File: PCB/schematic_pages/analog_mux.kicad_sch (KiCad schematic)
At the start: 33 parts, among them U1 SS49E, U10 SS49E, U11 SS49E, U12 SS49E, U13 SS49E, U3 SS49E, U4 SS49E, U5 SS49E, U6 SS49E, U7 SS49E, U8 SS49E, U9 SS49E

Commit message: repo rearrange
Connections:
- net MUX_IN_0 renamed AMUX_S0
- net MUX_IN_1 renamed AMUX_S1
- net MUX_IN_2 renamed AMUX_S2
- net MUX_IN_3 renamed AMUX_S3
- net MUX_OUT renamed AMUX_OUT
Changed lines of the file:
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@@
 		)
 	)
-	(global_label "MUX_IN_1"
+	(hierarchical_label "AMUX_OUT"
 		(shape input)
-		(at 25.4 102.87 180)
-		(fields_autoplaced yes)
+		(at 25.4 90.17 180)
 		(effects
 			(font
@@
 			(justify right)
 		)
-		(property "Intersheetrefs" "${INTERSHEET_REFS}"
-			(at 13.3434 102.87 0)
-			(effects
-				(font
-					(size 1.27 1.27)
-				)
-				(justify right)
-				(hide yes)
-			)
-		)
 	)
-	(global_label "MUX_OUT"
+	(hierarchical_label "AMUX_S1"
 		(shape input)
-		(at 25.4 90.17 180)
-		(fields_autoplaced yes)
+		(at 25.4 102.87 180)
 		(effects
 			(font
@@
 			(justify right)
 		)
-		(property "Intersheetrefs" "${INTERSHEET_REFS}"
-			(at 13.8272 90.17 0)
-			(effects
-				(font
-					(size 1.27 1.27)
-				)
-				(justify right)
-				(hide yes)
-			)
-		)
 	)
-	(global_label "MUX_IN_0"
+	(hierarchical_label "AMUX_S0"
 		(shape input)
 		(at 25.4 100.33 180)
-		(fields_autoplaced yes)
 		(effects
 			(font
@@
 			(justify right)
 		)
-		(property "Intersheetrefs" "${INTERSHEET_REFS}"
-			(at 13.3434 100.33 0)
-			(effects
-				(font
-					(size 1.27 1.27)
-				)
-				(justify right)
-				(hide yes)
-			)
-		)
 	)
-	(global_label "MUX_IN_3"
+	(hierarchical_label "AMUX_S2"
 		(shape input)
-		(at 25.4 107.95 180)
-		(fields_autoplaced yes)
+		(at 25.4 105.41 180)
 		(effects
 			(font
@@
 			(justify right)
 		)
-		(property "Intersheetrefs" "${INTERSHEET_REFS}"
-			(at 13.3434 107.95 0)
-			(effects
-				(font
-					(size 1.27 1.27)
-				)
-				(justify right)
-				(hide yes)
-			)
-		)
 	)
-	(global_label "MUX_IN_2"
+	(hierarchical_label "AMUX_S3"
 		(shape input)
-		(at 25.4 105.41 180)
-		(fields_autoplaced yes)
+		(at 25.4 107.95 180)
 		(effects
 			(font
@@
 			(justify right)
 		)
-		(property "Intersheetrefs" "${INTERSHEET_REFS}"
-			(at 13.3434 105.41 0)
-			(effects
-				(font
-					(size 1.27 1.27)
-				)
-				(justify right)
-				(hide yes)
-			)
-		)
 	)

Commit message: new schematics
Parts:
- removed U2: ~, symbol Symbols:CD74HC4067M Analog Mux
- added AM1: CD74HC4067M, Footprints:CD74HC4067M Analog Mux (SOIC-24), symbol Symbols:CD74HC4067M Analog Mux
- C30, C31, C32, C33, C34, C35, C36, C37, C38, C39, C40, C41: footprint (none) -> Footprints:0603_C
- R1, R2, R3, R4, R5, R6, R7, R8: footprint (none) -> Footprints:0603_R
- U1, U10, U11, U12, U13, U3, U4, U5, U6, U7, U8, U9: footprint (none) -> Footprints:SLSS49E-3 Hall Sensor (SOT-23-3)
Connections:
- net AMUX_OUT: now also AM1.1 (COM)
- net AMUX_S0: now also AM1.10 (S0)
- net AMUX_S1: now also AM1.11 (S1)
- net AMUX_S2: now also AM1.14 (S2)
- net AMUX_S3: now also AM1.13 (S3)
- net GND: now also AM1.12 (GND), AM1.15 (~{E})
- net VCC: now also AM1.24 (VCC)
- net at U13.2 (OUTPUT): now also AM1.20 (I11)
- net at U7.2 (OUTPUT): now also AM1.4 (I5)
- net at U10.2 (OUTPUT): now also AM1.23 (I8)
- net at U11.2 (OUTPUT): now also AM1.22 (I9)
- net at R4.1: now also AM1.18 (I13)
- net at U12.2 (OUTPUT): now also AM1.21 (I10)
- net at U9.2 (OUTPUT): now also AM1.2 (I7)
- net at R2.1: now also AM1.16 (I15)
- net at R3.1: now also AM1.17 (I14)
- net at R5.1: now also AM1.19 (I12)
- net at U8.2 (OUTPUT): now also AM1.3 (I6)
- net at U6.2 (OUTPUT): now also AM1.5 (I4)
- net at U5.2 (OUTPUT): now also AM1.6 (I3)
- net at U4.2 (OUTPUT): now also AM1.7 (I2)
- net at U3.2 (OUTPUT): now also AM1.8 (I1)
- net at U1.2 (OUTPUT): now also AM1.9 (I0)
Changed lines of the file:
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@@
 	)
 	(junction
+		(at 38.1 130.81)
+		(diameter 0)
+		(color 0 0 0 0)
+	)
+	(junction
 		(at 163.83 67.31)
 		(diameter 0)
@@
 	)
 	(junction
-		(at 38.1 130.81)
-		(diameter 0)
-		(color 0 0 0 0)
-	)
-	(junction
 		(at 245.11 72.39)
 		(diameter 0)
@@
 			)
 		)
-		(property "Footprint" ""
+		(property "Footprint" "Footprints:0603_C"
 			(at 62.23 67.31 0)
 			(effects
@@
 			)
 		)
-		(property "Footprint" ""
+		(property "Footprint" "Footprints:0603_C"
 			(at 176.53 67.31 0)
 			(effects
@@
 			)
 		)
-		(property "Footprint" ""
+		(property "Footprint" "Footprints:SLSS49E-3 Hall Sensor (SOT-23-3)"
 			(at 270.51 74.93 0)
 			(effects
@@
 			)
 		)
-		(property "Footprint" ""
+		(property "Footprint" "Footprints:SLSS49E-3 Hall Sensor (SOT-23-3)"
 			(at 157.48 74.93 0)
 			(effects
@@
 			)
 		)
-		(property "Footprint" ""
+		(property "Footprint" "Footprints:SLSS49E-3 Hall Sensor (SOT-23-3)"
 			(at 214.63 74.93 0)
 			(effects
@@
 	)
 	(symbol
+		(lib_id "Symbols:CD74HC4067M Analog Mux")
+		(at 38.1 104.14 0)
+		(unit 1)
+		(exclude_from_sim no)
+		(in_bom yes)
+		(on_board yes)
+		(dnp no)
+		(property "Reference" "AM1"
+			(at 36.83 104.394 0)
+			(effects
+				(font
+					(size 1.27 1.27)
+				)
+				(justify left)
+			)
+		)
+		(property "Value" "CD74HC4067M"
+			(at 38.1 104.14 0)
+			(effects
+				(font
+					(size 1.27 1.27)
+				)
+				(hide yes)
+			)
+		)
+		(property "Footprint" "Footprints:CD74HC4067M Analog Mux (SOIC-24)"
+			(at 38.1 104.14 0)
+			(effects
+				(font
+					(size 1.27 1.27)
+				)
+				(hide yes)
+			)
+		)
+		(property "Datasheet" ""
+			(at 38.1 104.14 0)
+			(effects
+				(font
+					(size 1.27 1.27)
+				)
+				(hide yes)
+			)
+		)
+		(property "Description" ""
+			(at 38.1 104.14 0)
+			(effects
+				(font
+					(size 1.27 1.27)
+				)
+				(hide yes)
+			)
+		)
+		(pin "1"
+		)
+		(pin "10"
+		)
+		(pin "11"
+		)
+		(pin "14"
+		)
+		(pin "13"
+		)
+		(pin "15"
+		)
+		(pin "24"
+		)
+		(pin "12"
+		)
+		(pin "9"
+		)
+		(pin "8"
+		)
+		(pin "7"
+		)
+		(pin "6"
+		)
+		(pin "5"
+		)
+		(pin "4"
+		)
+		(pin "3"
+		)
+		(pin "2"
+		)
+		(pin "23"
+		)
+		(pin "22"
+		)
+		(pin "21"
+		)
+		(pin "20"
+		)
+		(pin "19"
+		)
+		(pin "18"
+		)
+		(pin "17"
+		)
+		(pin "16"
+		)
+		(instances
+			(project ""
+				(path "/de43e009-b04c-42c1-b131-cdc664039a0d/333a86ff-2f60-4263-8580-754eb0fa7cf4"
+					(reference "AM1")
+					(unit 1)
+				)
+			)
+		)
+	)
+	(symbol
 		(lib_id "Symbols:GND")
 		(at 208.28 72.39 0)
@@
 			)
 		)
-		(property "Footprint" ""
+		(property "Footprint" "Footprints:SLSS49E-3 Hall Sensor (SOT-23-3)"
 			(at 233.68 74.93 0)
 			(effects
@@
 			)
 		)
-		(property "Footprint" ""
+		(property "Footprint" "Footprints:0603_R"
 			(at 57.15 118.11 0)
 			(effects
@@
 			)
 		)
-		(property "Footprint" ""
+		(property "Footprint" "Footprints:SLSS49E-3 Hall Sensor (SOT-23-3)"
 			(at 251.46 74.93 0)
 			(effects
@@
 			)
 		)
-		(property "Footprint" ""
+		(property "Footprint" "Footprints:SLSS49E-3 Hall Sensor (SOT-23-3)"
 			(at 195.58 74.93 0)
 			(effects
@@
 	)
 	(symbol
-		(lib_id "Symbols:CD74HC4067M Analog Mux")
-		(at 38.1 104.14 0)
-		(unit 1)
-		(exclude_from_sim no)
-		(in_bom yes)
-		(on_board yes)
-		(dnp no)
-		(property "Reference" "U2"
-			(at 40.132 79.248 0)
-			(effects
-				(font
-					(size 1.27 1.27)
-				)
-				(justify left)
-			)
-		)
-		(property "Value" "~"
-			(at 40.2433 78.74 0)
-			(effects
-				(font
-					(size 1.27 1.27)
-				)
-				(justify left)
-				(hide yes)
-			)
-		)
-		(property "Footprint" ""
-			(at 38.1 104.14 0)
-			(effects
-				(font
-					(size 1.27 1.27)
-				)
-				(hide yes)
-			)
-		)
-		(property "Datasheet" ""
-			(at 38.1 104.14 0)
-			(effects
-				(font
-					(size 1.27 1.27)
-				)
-				(hide yes)
-			)
-		)
-		(property "Description" ""
-			(at 38.1 104.14 0)
-			(effects
-				(font
-					(size 1.27 1.27)
-				)
-				(hide yes)
-			)
-		)
-		(pin "9"
-		)
-		(pin "2"
-		)
-		(pin "17"
-		)
-		(pin "11"
-		)
-		(pin "15"
-		)
-		(pin "18"
-		)
-		(pin "22"
-		)
-		(pin "4"
-		)
-		(pin "20"
-		)
-		(pin "7"
-		)
-		(pin "21"
-		)
-		(pin "24"
-		)
-		(pin "23"
-		)
-		(pin "8"
-		)
-		(pin "5"
-		)
-		(pin "6"
-		)
-		(pin "16"
-		)
-		(pin "19"
-		)
-		(pin "13"
-		)
-		(pin "14"
-		)
-		(pin "12"
-		)
-		(pin "10"
-		)
-		(pin "1"
-		)
-		(pin "3"
-		)
-		(instances
-			(project "pcb_schematics"
-				(path "/de43e009-b04c-42c1-b131-cdc664039a0d/333a86ff-2f60-4263-8580-754eb0fa7cf4"
-					(reference "U2")
-					(unit 1)
-				)
-			)
-		)
-	)
-	(symbol
 		(lib_id "Symbols:GND")
 		(at 245.11 72.39 0)
@@
 			)
 		)
-		(property "Footprint" ""
+		(property "Footprint" "Footprints:0603_R"
 			(at 57.15 123.19 0)
 			(effects
@@
 			)
 		)
-		(property "Footprint" ""
+		(property "Footprint" "Footprints:0603_C"
 			(at 233.68 67.31 0)
 			(effects
@@
 			)
 		)
-		(property "Footprint" ""
+		(property "Footprint" "Footprints:0603_C"
 			(at 195.58 67.31 0)
 			(effects
@@
 			)
 		)
-		(property "Footprint" ""
+		(property "Footprint" "Footprints:0603_C"
 			(at 100.33 67.31 0)
 			(effects
@@
 			)
 		)
-		(property "Footprint" ""
+		(property "Footprint" "Footprints:SLSS49E-3 Hall Sensor (SOT-23-3)"
 			(at 81.28 74.93 0)
 			(effects
@@
 			)
 		)
-		(property "Footprint" ""
+		(property "Footprint" "Footprints:SLSS49E-3 Hall Sensor (SOT-23-3)"
 			(at 62.23 74.93 0)
 			(effects
@@
 			)
 		)
-		(property "Footprint" ""
+		(property "Footprint" "Footprints:0603_C"
 			(at 157.48 67.31 0)
 			(effects
@@
 			)
 		)
-		(property "Footprint" ""
+		(property "Footprint" "Footprints:SLSS49E-3 Hall Sensor (SOT-23-3)"
 			(at 138.43 74.93 0)
 			(effects
@@
 			)
 		)
-		(property "Footprint" ""
+		(property "Footprint" "Footprints:SLSS49E-3 Hall Sensor (SOT-23-3)"
 			(at 119.38 74.93 0)
 			(effects
@@
 			)
 		)
-		(property "Footprint" ""
+		(property "Footprint" "Footprints:0603_C"
 			(at 214.63 67.31 0)
 			(effects
@@
 			)
 		)
-		(property "Footprint" ""
+		(property "Footprint" "Footprints:SLSS49E-3 Hall Sensor (SOT-23-3)"
 			(at 176.53 74.93 0)
 			(effects
@@
 			)
 		)
-		(property "Footprint" ""
+		(property "Footprint" "Footprints:0603_C"
 			(at 81.28 67.31 0)
 			(effects
@@
 			)
 		)
-		(property "Footprint" ""
+		(property "Footprint" "Footprints:0603_R"
 			(at 104.14 137.16 0)
 			(effects
@@
 			)
 		)
-		(property "Footprint" ""
+		(property "Footprint" "Footprints:SLSS49E-3 Hall Sensor (SOT-23-3)"
 			(at 100.33 74.93 0)
 			(effects
@@
 			)
 		)
-		(property "Footprint" ""
+		(property "Footprint" "Footprints:0603_R"
 			(at 62.23 137.16 0)
 			(effects
@@
 			)
 		)
-		(property "Footprint" ""
+		(property "Footprint" "Footprints:0603_C"
 			(at 138.43 67.31 0)
 			(effects
@@
 			)
 		)
-		(property "Footprint" ""
+		(property "Footprint" "Footprints:0603_R"
 			(at 76.2 137.16 0)
 			(effects
@@
 			)
 		)
-		(property "Footprint" ""
+		(property "Footprint" "Footprints:0603_C"
 			(at 119.38 67.31 0)
 			(effects
@@
 			)
 		)
-		(property "Footprint" ""
+		(property "Footprint" "Footprints:0603_R"
 			(at 57.15 120.65 0)
 			(effects
@@
 			)
 		)
-		(property "Footprint" ""
+		(property "Footprint" "Footprints:0603_R"
 			(at 57.15 115.57 0)
 			(effects
@@
 			)
 		)
-		(property "Footprint" ""
+		(property "Footprint" "Footprints:0603_R"
 			(at 90.17 137.16 0)
 			(effects
@@
 			)
 		)
-		(property "Footprint" ""
+		(property "Footprint" "Footprints:0603_C"
 			(at 270.51 67.31 0)
 			(effects
@@
 			)
 		)
-		(property "Footprint" ""
+		(property "Footprint" "Footprints:0603_C"
 			(at 251.46 67.31 0)
 			(effects

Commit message: pcbing
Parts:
- renumbered U11 to U10, U12 to U11, U13 to U12, U3 to U2, U4 to U3, U5 to U4, U6 to U5, U7 to U6, U8 to U7, U9 to U8, U10 to U9
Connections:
- net GND: now also U1.2 (GND), U10.2 (GND), U11.2 (GND), U12.2 (GND), U2.2 (GND), U3.2 (GND), U4.2 (GND), U5.2 (GND), U6.2 (GND), U7.2 (GND), U8.2 (GND), U9.2 (GND); no longer U1.3 (GND), U10.3 (GND), U11.3 (GND), U12.3 (GND), U2.3 (GND), U3.3 (GND), U4.3 (GND), U5.3 (GND), U6.3 (GND), U7.3 (GND), U8.3 (GND), U9.3 (GND)
- net at AM1.20 (I11): now also U12.3 (OUTPUT); no longer U12.2 (OUTPUT)
- net at AM1.4 (I5): now also U6.3 (OUTPUT); no longer U6.2 (OUTPUT)
- net at AM1.23 (I8): now also U9.3 (OUTPUT); no longer U9.2 (OUTPUT)
- net at AM1.2 (I7): now also U8.3 (OUTPUT); no longer U8.2 (OUTPUT)
- net at AM1.21 (I10): now also U11.3 (OUTPUT); no longer U11.2 (OUTPUT)
- net at AM1.22 (I9): now also U10.3 (OUTPUT); no longer U10.2 (OUTPUT)
- net at AM1.3 (I6): now also U7.3 (OUTPUT); no longer U7.2 (OUTPUT)
- net at AM1.5 (I4): now also U5.3 (OUTPUT); no longer U5.2 (OUTPUT)
- net at AM1.6 (I3): now also U4.3 (OUTPUT); no longer U4.2 (OUTPUT)
- net at AM1.7 (I2): now also U3.3 (OUTPUT); no longer U3.2 (OUTPUT)
- net at AM1.8 (I1): now also U2.3 (OUTPUT); no longer U2.2 (OUTPUT)
- net at AM1.9 (I0): now also U1.3 (OUTPUT); no longer U1.2 (OUTPUT)
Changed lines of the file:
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@@
 		(on_board yes)
 		(dnp no)
-		(property "Reference" "U13"
+		(property "Reference" "U12"
 			(at 277.876 75.946 0)
 			(effects
@@
 			(project "pcb_schematics"
 				(path "/de43e009-b04c-42c1-b131-cdc664039a0d/333a86ff-2f60-4263-8580-754eb0fa7cf4"
-					(reference "U13")
+					(reference "U12")
 					(unit 1)
 				)
@@
 		(on_board yes)
 		(dnp no)
-		(property "Reference" "U7"
+		(property "Reference" "U6"
 			(at 164.846 75.946 0)
 			(effects
@@
 			(project "pcb_schematics"
 				(path "/de43e009-b04c-42c1-b131-cdc664039a0d/333a86ff-2f60-4263-8580-754eb0fa7cf4"
-					(reference "U7")
+					(reference "U6")
 					(unit 1)
 				)
@@
 		(on_board yes)
 		(dnp no)
-		(property "Reference" "U10"
+		(property "Reference" "U9"
 			(at 221.996 75.946 0)
 			(effects
@@
 			(project "pcb_schematics"
 				(path "/de43e009-b04c-42c1-b131-cdc664039a0d/333a86ff-2f60-4263-8580-754eb0fa7cf4"
-					(reference "U10")
+					(reference "U9")
 					(unit 1)
 				)
@@
 		(on_board yes)
 		(dnp no)
-		(property "Reference" "U11"
+		(property "Reference" "U10"
 			(at 241.046 75.946 0)
 			(effects
@@
 			(project "pcb_schematics"
 				(path "/de43e009-b04c-42c1-b131-cdc664039a0d/333a86ff-2f60-4263-8580-754eb0fa7cf4"
-					(reference "U11")
+					(reference "U10")
 					(unit 1)
 				)
@@
 		(on_board yes)
 		(dnp no)
-		(property "Reference" "U12"
+		(property "Reference" "U11"
 			(at 258.826 75.946 0)
 			(effects
@@
 			(project "pcb_schematics"
 				(path "/de43e009-b04c-42c1-b131-cdc664039a0d/333a86ff-2f60-4263-8580-754eb0fa7cf4"
-					(reference "U12")
+					(reference "U11")
 					(unit 1)
 				)
@@
 		(on_board yes)
 		(dnp no)
-		(property "Reference" "U9"
+		(property "Reference" "U8"
 			(at 202.946 75.946 0)
 			(effects
@@
 			(project "pcb_schematics"
 				(path "/de43e009-b04c-42c1-b131-cdc664039a0d/333a86ff-2f60-4263-8580-754eb0fa7cf4"
-					(reference "U9")
+					(reference "U8")
 					(unit 1)
 				)
@@
 		(on_board yes)
 		(dnp no)
-		(property "Reference" "U3"
+		(property "Reference" "U2"
 			(at 88.646 75.946 0)
 			(effects
@@
 			(project "pcb_schematics"
 				(path "/de43e009-b04c-42c1-b131-cdc664039a0d/333a86ff-2f60-4263-8580-754eb0fa7cf4"
-					(reference "U3")
+					(reference "U2")
 					(unit 1)
 				)
@@
 		(on_board yes)
 		(dnp no)
-		(property "Reference" "U6"
+		(property "Reference" "U5"
 			(at 145.796 75.946 0)
 			(effects
@@
 			(project "pcb_schematics"
 				(path "/de43e009-b04c-42c1-b131-cdc664039a0d/333a86ff-2f60-4263-8580-754eb0fa7cf4"
-					(reference "U6")
+					(reference "U5")
 					(unit 1)
 				)
@@
 		(on_board yes)
 		(dnp no)
-		(property "Reference" "U5"
+		(property "Reference" "U4"
 			(at 126.746 75.946 0)
 			(effects
@@
 			(project "pcb_schematics"
 				(path "/de43e009-b04c-42c1-b131-cdc664039a0d/333a86ff-2f60-4263-8580-754eb0fa7cf4"
-					(reference "U5")
+					(reference "U4")
 					(unit 1)
 				)
@@
 		(on_board yes)
 		(dnp no)
-		(property "Reference" "U8"
+		(property "Reference" "U7"
 			(at 183.896 75.946 0)
 			(effects
@@
 			(project "pcb_schematics"
 				(path "/de43e009-b04c-42c1-b131-cdc664039a0d/333a86ff-2f60-4263-8580-754eb0fa7cf4"
-					(reference "U8")
+					(reference "U7")
 					(unit 1)
 				)
@@
 		(on_board yes)
 		(dnp no)
-		(property "Reference" "U4"
+		(property "Reference" "U3"
 			(at 107.696 75.946 0)
 			(effects
@@
 			(project "pcb_schematics"
 				(path "/de43e009-b04c-42c1-b131-cdc664039a0d/333a86ff-2f60-4263-8580-754eb0fa7cf4"
-					(reference "U4")
-					(unit 1)
-				)
+					(reference "U3")
+					(unit 1)
+				)

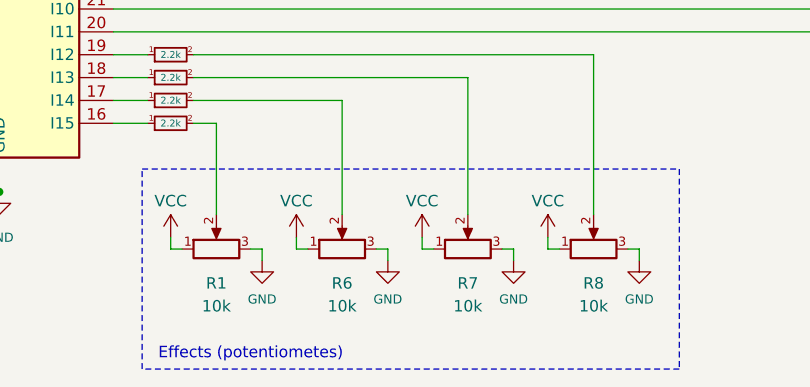
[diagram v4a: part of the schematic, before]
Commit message: led chain
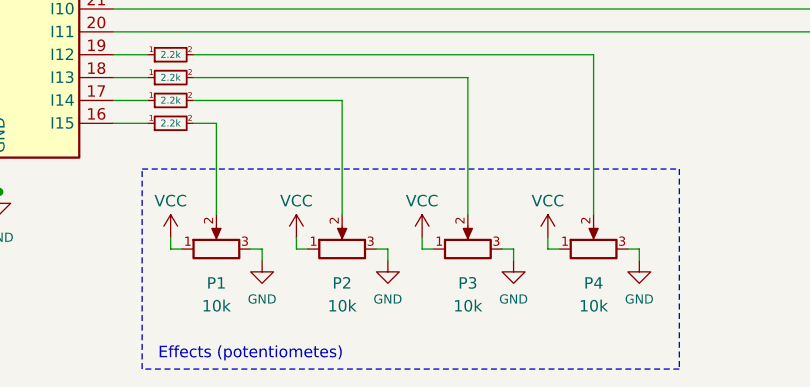
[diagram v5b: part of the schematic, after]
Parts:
- P1: renamed from R1; footprint Footprints:0603_R -> Footprints:Rotary Potentiometer RK09
- P2: renamed from R6; footprint Footprints:0603_R -> Footprints:Rotary Potentiometer RK09
- P3: renamed from R7; footprint Footprints:0603_R -> Footprints:Rotary Potentiometer RK09
- P4: renamed from R8; footprint Footprints:0603_R -> Footprints:Rotary Potentiometer RK09
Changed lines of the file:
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@@
 		(dnp no)
 		(fields_autoplaced yes)
-		(property "Reference" "R8"
+		(property "Reference" "P4"
 			(at 104.14 140.97 90)
 			(effects
@@
 			)
 		)
-		(property "Footprint" "Footprints:0603_R"
+		(property "Footprint" "Footprints:Rotary Potentiometer RK09"
 			(at 104.14 137.16 0)
 			(effects
@@
 			(project "pcb_schematics"
 				(path "/de43e009-b04c-42c1-b131-cdc664039a0d/333a86ff-2f60-4263-8580-754eb0fa7cf4"
-					(reference "R8")
+					(reference "P4")
 					(unit 1)
 				)
@@
 		(dnp no)
 		(fields_autoplaced yes)
-		(property "Reference" "R1"
+		(property "Reference" "P1"
 			(at 62.23 140.97 90)
 			(effects
@@
 			)
 		)
-		(property "Footprint" "Footprints:0603_R"
+		(property "Footprint" "Footprints:Rotary Potentiometer RK09"
 			(at 62.23 137.16 0)
 			(effects
@@
 			(project "pcb_schematics"
 				(path "/de43e009-b04c-42c1-b131-cdc664039a0d/333a86ff-2f60-4263-8580-754eb0fa7cf4"
-					(reference "R1")
+					(reference "P1")
 					(unit 1)
 				)
@@
 		(dnp no)
 		(fields_autoplaced yes)
-		(property "Reference" "R6"
+		(property "Reference" "P2"
 			(at 76.2 140.97 90)
 			(effects
@@
 			)
 		)
-		(property "Footprint" "Footprints:0603_R"
+		(property "Footprint" "Footprints:Rotary Potentiometer RK09"
 			(at 76.2 137.16 0)
 			(effects
@@
 			(project "pcb_schematics"
 				(path "/de43e009-b04c-42c1-b131-cdc664039a0d/333a86ff-2f60-4263-8580-754eb0fa7cf4"
-					(reference "R6")
+					(reference "P2")
 					(unit 1)
 				)
@@
 		(dnp no)
 		(fields_autoplaced yes)
-		(property "Reference" "R7"
+		(property "Reference" "P3"
 			(at 90.17 140.97 90)
 			(effects
@@
 			)
 		)
-		(property "Footprint" "Footprints:0603_R"
+		(property "Footprint" "Footprints:Rotary Potentiometer RK09"
 			(at 90.17 137.16 0)
 			(effects
@@
 			(project "pcb_schematics"
 				(path "/de43e009-b04c-42c1-b131-cdc664039a0d/333a86ff-2f60-4263-8580-754eb0fa7cf4"
-					(reference "R7")
-					(unit 1)
-				)
+					(reference "P3")
+					(unit 1)
+				)
